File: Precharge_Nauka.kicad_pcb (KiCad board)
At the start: 2 copper layers, 33 parts, among them Q1 C2M0280120D, Q2 C2M0280120D, Q3 C2M0280120D, Q4 2N7002, Q5 C2M0280120D

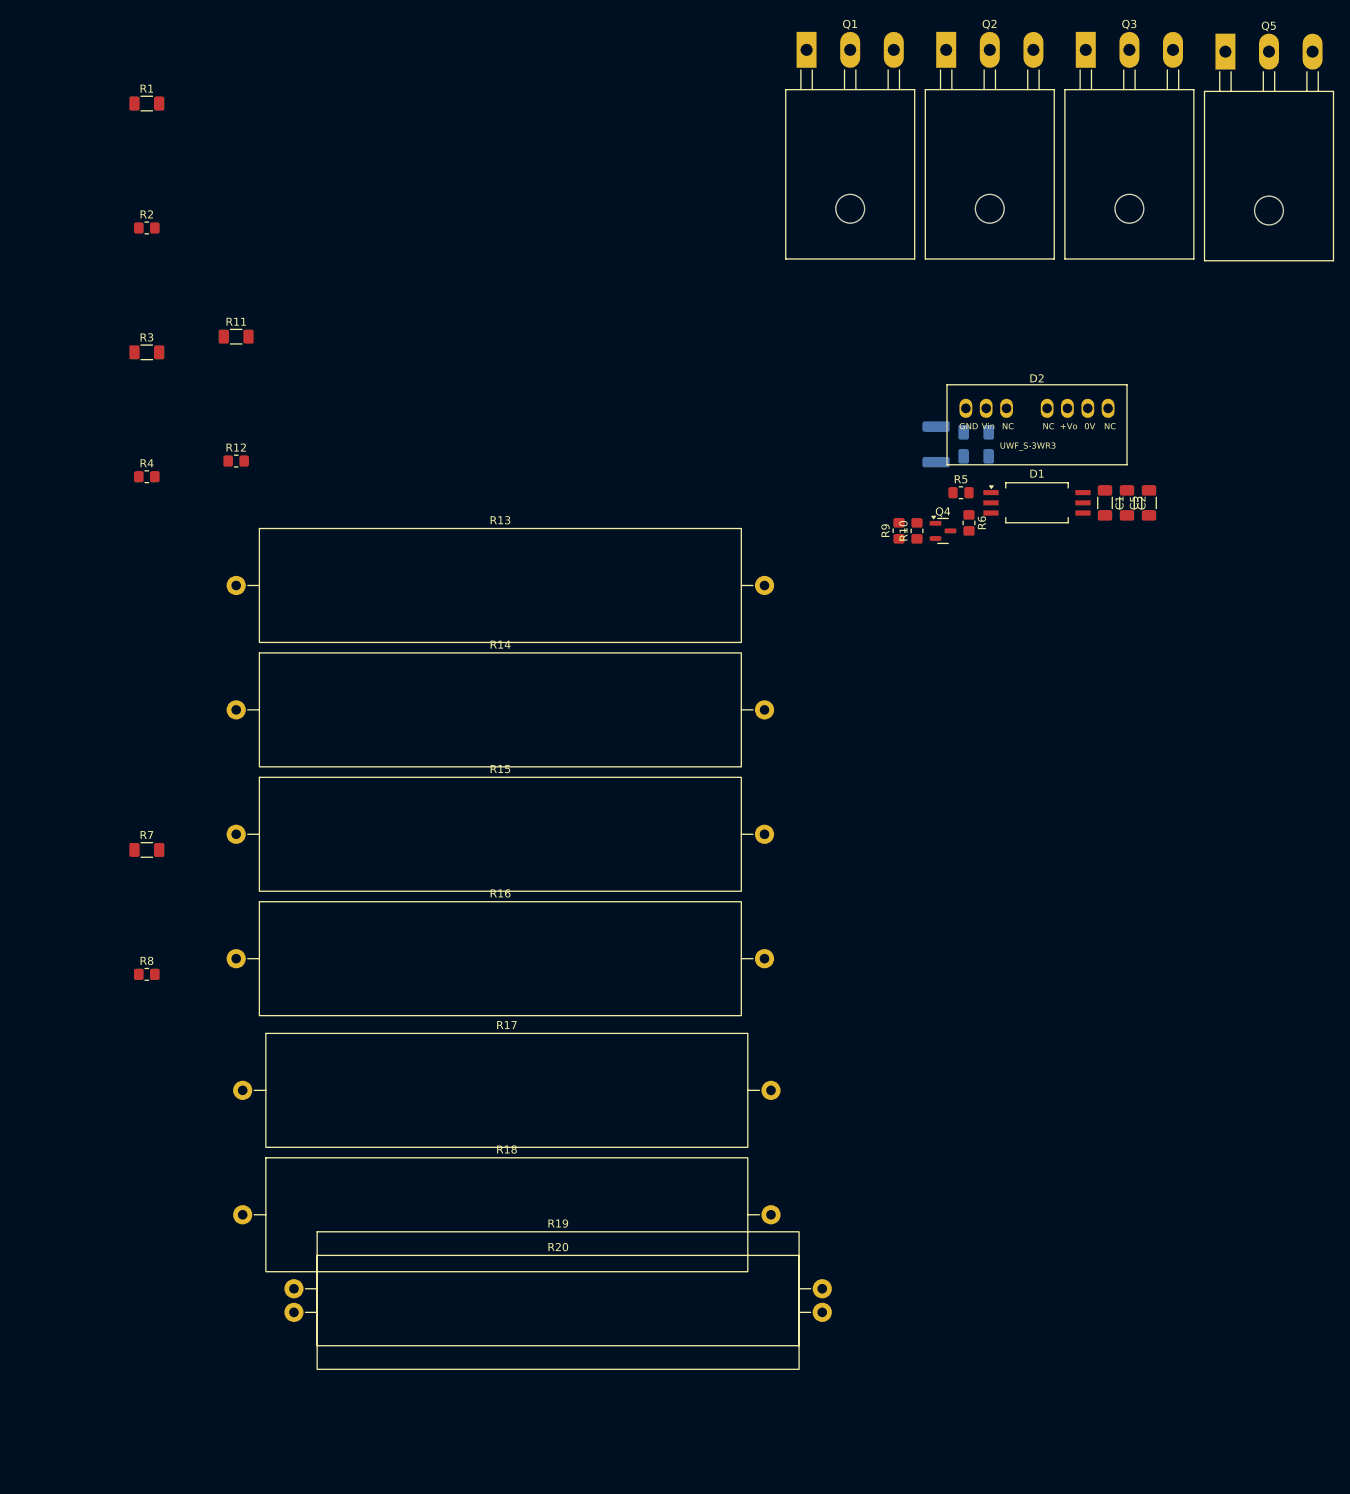
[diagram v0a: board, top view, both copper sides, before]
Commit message: VER1.0: закончил основную схему и раскидал на плате
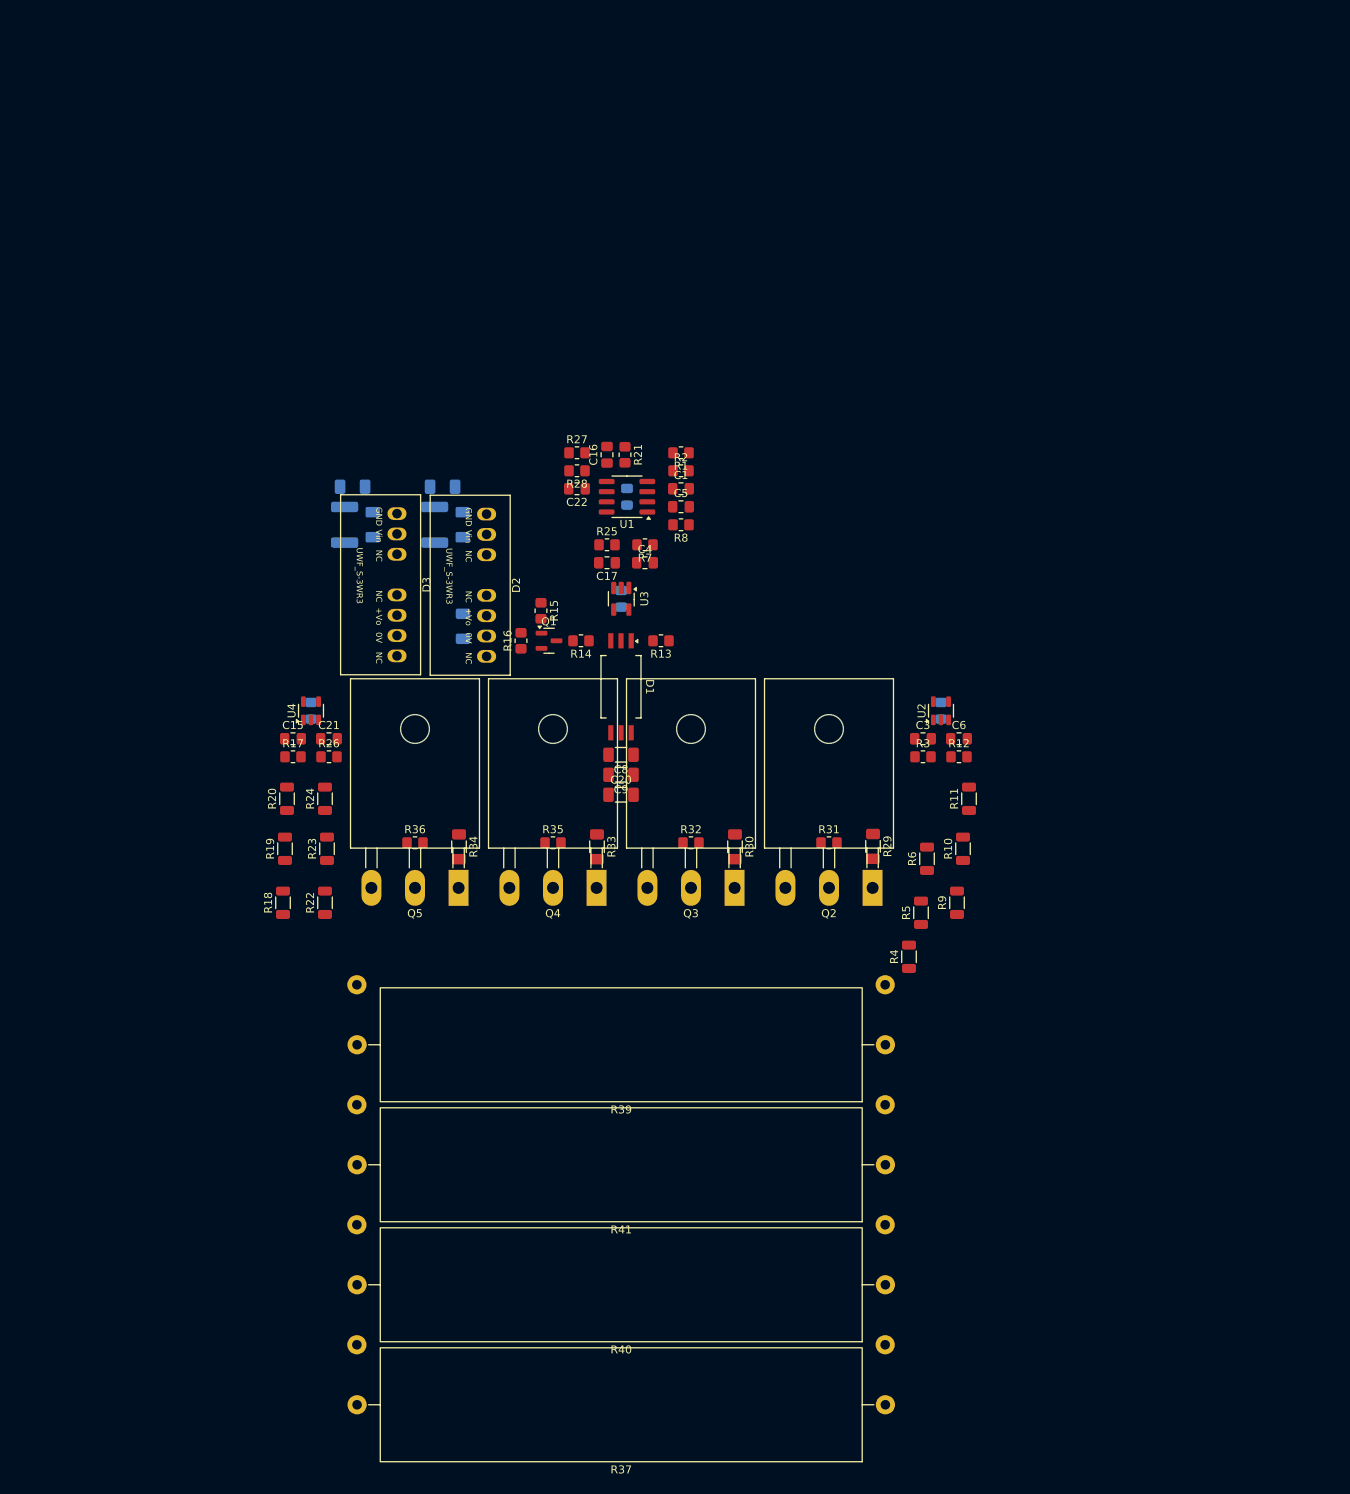
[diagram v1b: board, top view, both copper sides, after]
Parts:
- added C10: 1u, Capacitor_SMD:C_0805_2012Metric_Pad1.18x1.45mm_HandSolder, B.Cu at (186.8, 131.2)
- added C11: 10u, Capacitor_SMD:C_1206_3216Metric_Pad1.33x1.80mm_HandSolder, B.Cu at (163.7, 130.0)
- added C12: 10u, Capacitor_SMD:C_1206_3216Metric_Pad1.33x1.80mm_HandSolder, B.Cu at (166.2, 134.8)
- added C13: 22u, Capacitor_SMD:C_1206_3216Metric_Pad1.33x1.80mm_HandSolder, B.Cu at (166.2, 147.4)
- added C14: 100n, Capacitor_SMD:C_0805_2012Metric_Pad1.18x1.45mm_HandSolder, B.Cu at (147.2, 158.0)
- added C15: 10n, Capacitor_SMD:C_0805_2012Metric_Pad1.18x1.45mm_HandSolder, F.Cu at (145.0, 161.5)
- added C16: 100n, Capacitor_SMD:C_0805_2012Metric_Pad1.18x1.45mm_HandSolder, F.Cu at (184.2, 126.0)
- added C17: 100n, Capacitor_SMD:C_0805_2012Metric_Pad1.18x1.45mm_HandSolder, F.Cu at (184.2, 139.5)
- added C18: 10u, Capacitor_SMD:C_1206_3216Metric_Pad1.33x1.80mm_HandSolder, B.Cu at (152.4, 130.0)
- added C19: 10u, Capacitor_SMD:C_1206_3216Metric_Pad1.33x1.80mm_HandSolder, B.Cu at (154.9, 134.8)
- added C20: 22u, Capacitor_SMD:C_1206_3216Metric_Pad1.33x1.80mm_HandSolder, F.Cu at (186.0, 168.5)
- added C21: 10n, Capacitor_SMD:C_0805_2012Metric_Pad1.18x1.45mm_HandSolder, F.Cu at (149.5, 161.5)
- added C22: 1u, Capacitor_SMD:C_0805_2012Metric_Pad1.18x1.45mm_HandSolder, F.Cu at (180.5, 130.2)
- added C6: 10n, Capacitor_SMD:C_0805_2012Metric_Pad1.18x1.45mm_HandSolder, F.Cu at (228.2, 161.5)
- added C7: 1u, Capacitor_SMD:C_0805_2012Metric_Pad1.18x1.45mm_HandSolder, B.Cu at (186.0, 144.0)
- added C8: 0.1u, Capacitor_SMD:C_1206_3216Metric_Pad1.33x1.80mm_HandSolder, F.Cu at (186.0, 163.5)
- added C9: 10u, Capacitor_SMD:C_1206_3216Metric_Pad1.33x1.80mm_HandSolder, F.Cu at (186.0, 166.0)
- added D3: UWF1215S-3WR3, MORNSUN:UWF_S-3WR3, F.Cu at (158.0, 142.2)
- added L2: 22u, Inductor_SMD:L_1812_4532Metric_Pad1.30x3.40mm_HandSolder, B.Cu at (151.4, 134.8)
- added R21: 120, Resistor_SMD:R_0805_2012Metric_Pad1.20x1.40mm_HandSolder, F.Cu at (186.5, 126.0)
- added R22: 330k, Resistor_SMD:R_1206_3216Metric, F.Cu at (149.0, 182.0)
- added R23: 330k, Resistor_SMD:R_1206_3216Metric, F.Cu at (149.2, 175.2)
- added R24: 330k, Resistor_SMD:R_1206_3216Metric, F.Cu at (149.0, 169.0)
- added R25: 120, Resistor_SMD:R_0805_2012Metric_Pad1.20x1.40mm_HandSolder, F.Cu at (184.2, 137.2)
- added R26: 10k, Resistor_SMD:R_0805_2012Metric_Pad1.20x1.40mm_HandSolder, F.Cu at (149.5, 163.8)
- added R27: 12.1k, Resistor_SMD:R_0805_2012Metric_Pad1.20x1.40mm_HandSolder, F.Cu at (180.5, 125.8)
- added R28: 56k, Resistor_SMD:R_0805_2012Metric_Pad1.20x1.40mm_HandSolder, F.Cu at (180.5, 128.0)
- added R29: 15, Resistor_SMD:R_1206_3216Metric_Pad1.30x1.75mm_HandSolder, F.Cu at (217.5, 174.9)
- added R30: 15, Resistor_SMD:R_1206_3216Metric_Pad1.30x1.75mm_HandSolder, F.Cu at (200.2, 175.0)
- added R31: 10k, Resistor_SMD:R_0805_2012Metric_Pad1.20x1.40mm_HandSolder, F.Cu at (212.0, 174.5)
- added R32: 10k, Resistor_SMD:R_0805_2012Metric_Pad1.20x1.40mm_HandSolder, F.Cu at (194.8, 174.5)
- added R33: 15, Resistor_SMD:R_1206_3216Metric_Pad1.30x1.75mm_HandSolder, F.Cu at (183.0, 175.0)
- added R34: 15, Resistor_SMD:R_1206_3216Metric_Pad1.30x1.75mm_HandSolder, F.Cu at (165.8, 175.0)
- added R35: 10k, Resistor_SMD:R_0805_2012Metric_Pad1.20x1.40mm_HandSolder, F.Cu at (177.5, 174.5)
- added R36: 10k, Resistor_SMD:R_0805_2012Metric_Pad1.20x1.40mm_HandSolder, F.Cu at (160.2, 174.5)
- added R37: 10k, Resistor_THT:R_Axial_Power_L60.0mm_W14.0mm_P66.04mm, F.Cu at (219.1, 244.8)
- added R38: 10k, Resistor_THT:R_Axial_Power_L60.0mm_W14.0mm_P66.04mm, B.Cu at (219.0, 237.2)
- added R39: 10k, Resistor_THT:R_Axial_Power_L60.0mm_W14.0mm_P66.04mm, F.Cu at (219.1, 199.8)
- added R40: 10k, Resistor_THT:R_Axial_Power_L60.0mm_W14.0mm_P66.04mm, F.Cu at (219.1, 229.8)
- added R41: 10k, Resistor_THT:R_Axial_Power_L60.0mm_W14.0mm_P66.04mm, F.Cu at (219.1, 214.8)
- added R42: 10k, Resistor_THT:R_Axial_Power_L60.0mm_W14.0mm_P66.04mm, B.Cu at (219.0, 207.2)
- added R43: 10k, Resistor_THT:R_Axial_Power_L60.0mm_W14.0mm_P66.04mm, B.Cu at (219.0, 192.2)
- added R44: 10k, Resistor_THT:R_Axial_Power_L60.0mm_W14.0mm_P66.04mm, B.Cu at (219.0, 222.2)
- added U1: LM2903, Package_SO:SOP-8_3.76x4.96mm_P1.27mm, F.Cu at (186.8, 131.2)
- added U2: LMV321IDBVR, Package_TO_SOT_SMD:SOT-23-5, F.Cu at (226.0, 158.0)
- added U3: 74LVC1G08, Package_TO_SOT_SMD:SOT-23-5_HandSoldering, F.Cu at (186.0, 144.0)
- added U4: LMV321IDBVR, Package_TO_SOT_SMD:SOT-23-5, F.Cu at (147.2, 158.0)
- C1: value 0.1u -> 1u; footprint Capacitor_SMD:C_1206_3216Metric_Pad1.33x1.80mm_HandSolder -> Capacitor_SMD:C_0805_2012Metric_Pad1.18x1.45mm_HandSolder
- C2: value 10u -> 100n; footprint Capacitor_SMD:C_1206_3216Metric_Pad1.33x1.80mm_HandSolder -> Capacitor_SMD:C_0805_2012Metric_Pad1.18x1.45mm_HandSolder; moved to B.Cu
- C3: value 10u -> 10n; footprint Capacitor_SMD:C_1206_3216Metric_Pad1.33x1.80mm_HandSolder -> Capacitor_SMD:C_0805_2012Metric_Pad1.18x1.45mm_HandSolder; moved to F.Cu
- C4: value 10u -> 100n; footprint Capacitor_SMD:C_1206_3216Metric_Pad1.33x1.80mm_HandSolder -> Capacitor_SMD:C_0805_2012Metric_Pad1.18x1.45mm_HandSolder; moved to F.Cu
- C5: value 22u -> 100n; footprint Capacitor_SMD:C_1206_3216Metric_Pad1.33x1.80mm_HandSolder -> Capacitor_SMD:C_0805_2012Metric_Pad1.18x1.45mm_HandSolder
- D2: value ~ -> UWF1205S-3WR3
- Q1: value C2M0280120D -> 2N7002; footprint Package_TO_SOT_THT:TO-247-3_Horizontal_TabUp -> Package_TO_SOT_SMD:SOT-23
- Q4: value 2N7002 -> C2M0280120D; footprint Package_TO_SOT_SMD:SOT-23 -> Package_TO_SOT_THT:TO-247-3_Horizontal_TabUp
- R1: value 15 -> 12.1k; footprint Resistor_SMD:R_1206_3216Metric_Pad1.30x1.75mm_HandSolder -> Resistor_SMD:R_0805_2012Metric_Pad1.20x1.40mm_HandSolder
- R10, R4: value 10k -> 330k; footprint Resistor_SMD:R_0805_2012Metric_Pad1.20x1.40mm_HandSolder -> Resistor_SMD:R_1206_3216Metric
- R11: value 15 -> 330k; footprint Resistor_SMD:R_1206_3216Metric_Pad1.30x1.75mm_HandSolder -> Resistor_SMD:R_1206_3216Metric
- R13, R14: value 10k -> 250; footprint Resistor_THT:R_Axial_Power_L60.0mm_W14.0mm_P66.04mm -> Resistor_SMD:R_0805_2012Metric_Pad1.20x1.40mm_HandSolder
- R15: value 10k -> 1; footprint Resistor_THT:R_Axial_Power_L60.0mm_W14.0mm_P66.04mm -> Resistor_SMD:R_0805_2012Metric_Pad1.20x1.40mm_HandSolder
- R16, R17: footprint Resistor_THT:R_Axial_Power_L60.0mm_W14.0mm_P66.04mm -> Resistor_SMD:R_0805_2012Metric_Pad1.20x1.40mm_HandSolder
- R18, R19, R20: value 10k -> 330k; footprint Resistor_THT:R_Axial_Power_L60.0mm_W14.0mm_P66.04mm -> Resistor_SMD:R_1206_3216Metric
- R2: value 10k -> 1.2k
- R3: value 15 -> 10k; footprint Resistor_SMD:R_1206_3216Metric_Pad1.30x1.75mm_HandSolder -> Resistor_SMD:R_0805_2012Metric_Pad1.20x1.40mm_HandSolder
- R5, R6: value 1.5k -> 330k; footprint Resistor_SMD:R_0805_2012Metric_Pad1.20x1.40mm_HandSolder -> Resistor_SMD:R_1206_3216Metric
- R7: value 15 -> 120; footprint Resistor_SMD:R_1206_3216Metric_Pad1.30x1.75mm_HandSolder -> Resistor_SMD:R_0805_2012Metric_Pad1.20x1.40mm_HandSolder
- R8: value 10k -> 120
- R9: value 1 -> 330k; footprint Resistor_SMD:R_0805_2012Metric_Pad1.20x1.40mm_HandSolder -> Resistor_SMD:R_1206_3216Metric
- moved Q5 141.8 mm to (165.7, 180.1), turned to 180 degrees
- moved Q3 113.6 mm to (200.2, 180.1), turned to 180 degrees
- moved R4 112.6 mm to (222.0, 188.8), turned to 90 degrees
- moved R3 109.4 mm to (223.8, 163.8)
- moved R11 108.3 mm to (229.5, 169.0), turned to 90 degrees
- moved Q2 105.2 mm to (217.4, 180.1), turned to 180 degrees
- moved R12 97.6 mm to (228.2, 163.8)
- moved R8 87.3 mm to (193.5, 134.8), turned to 180 degrees
- moved Q1 80.6 mm to (177.0, 149.2)
- moved R1 79.8 mm to (193.5, 125.8), turned to 180 degrees
- moved R2 73.3 mm to (193.5, 128.0)
- moved R7 73.0 mm to (189.0, 137.2), turned to 180 degrees
- moved D2 72.3 mm to (169.2, 142.3), turned to -90 degrees
- moved R20 64.2 mm to (144.2, 169.0), turned to 90 degrees
- moved L1 63.5 mm to (162.7, 134.8)
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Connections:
- C1 pad 1: VCC -> Net-(U1A-+)
- C1 pad 2: VDC_OUT -> GND1
- C2 pad 1: VCC -> +5V
- C2 pad 2: VDC_OUT -> GND1
- C3 pad 1: Net-(D2-GND) -> GND1
- C3 pad 2: GND -> Net-(U2-+)
- C4 pad 1: +27V -> Net-(C4-Pad1)
- C4 pad 2: GND -> GND1
- C5 pad 1: VDC_OUT -> Net-(U1A--)
- C5 pad 2: VCC -> GND1
- D2 pad 1: Net-(D2-GND) -> GND
- D2 pad 2: GND -> Net-(D2-Vin)
- D2 pad 6: VCC -> +5V
- D2 pad 7: VDC_OUT -> GND1
- L1 pad 1: +27V -> Net-(D2-Vin)
- L1 pad 2: Net-(D2-GND) -> +27V
- Q1 pad 2: VDC_IN -> GND1
- Q1 pad 3: VDC_OUT -> Net-(Q1-D)
- Q4 pad 2: GND -> VDC_IN
- Q4 pad 3: Net-(Q4-D) -> VDC_OUT
- R1 pad 1: Gate -> +5V
- R1 pad 2: Net-(Q1-G) -> Net-(U1A-+)
- R10 pad 1: GND -> Net-(R10-Pad1)
- R10 pad 2: Net-(Q4-G) -> Net-(R10-Pad2)
- R11 pad 1: Gate -> Net-(R10-Pad2)
- R11 pad 2: Net-(Q5-G) -> Net-(U2--)
- R12 pad 1: VDC_OUT -> Net-(U2--)
- R12 pad 2: Net-(Q5-G) -> Net-(C6-Pad2)
- R13 pad 1: VDC_IN -> +5V
- R13 pad 2: VDC_OUT -> Net-(D1-ANODE)
- R14 pad 1: VDC_IN -> Net-(D1-CATHODE)
- R14 pad 2: VDC_OUT -> Net-(Q1-D)
- R15 pad 1: VDC_IN -> Shunt_ON
- R15 pad 2: VDC_OUT -> Net-(Q1-G)
- R16 pad 1: VDC_IN -> GND1
- R16 pad 2: VDC_OUT -> Net-(Q1-G)
- R17 pad 1: VDC_IN -> GND1
- R17 pad 2: VDC_OUT -> Net-(U4-+)
- R18 pad 1: VDC_IN -> VDC_OUT
- R18 pad 2: VDC_OUT -> Net-(R18-Pad2)
- R19 pad 1: VDC_IN -> Net-(R18-Pad2)
- R19 pad 2: VDC_OUT -> Net-(R19-Pad2)
- R2 pad 1: VDC_OUT -> Net-(U1A-+)
- R2 pad 2: Net-(Q1-G) -> GND1
- R20 pad 1: VDC_IN -> Net-(R19-Pad2)
- R20 pad 2: VDC_OUT -> Net-(U4-+)
- R3 pad 1: Gate -> GND1
- R3 pad 2: Net-(Q2-G) -> Net-(U2-+)
- R4 pad 1: VDC_OUT -> VDC_IN
- R4 pad 2: Net-(Q2-G) -> Net-(R4-Pad2)
- R5 pad 1: +27V -> Net-(R4-Pad2)
- R5 pad 2: Net-(D1-ANODE) -> Net-(R5-Pad2)
- R6 pad 1: Net-(D1-CATHODE) -> Net-(R5-Pad2)
- R6 pad 2: Net-(Q4-D) -> Net-(U2-+)
- R7 pad 1: Gate -> Net-(R7-Pad1)
- R7 pad 2: Net-(Q3-G) -> Net-(C4-Pad1)
- R8 pad 1: VDC_OUT -> Net-(C6-Pad2)
- R8 pad 2: Net-(Q3-G) -> Net-(U1A--)
- R9 pad 1: Shunt_ON -> VDC_OUT
- R9 pad 2: Net-(Q4-G) -> Net-(R10-Pad1)
